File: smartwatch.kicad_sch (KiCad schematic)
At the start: 48 parts, among them IC1 W25N01GVZEIG, IC2 NORA-B120-00B, J1 Charging_Pad-, J2 Charging_Pad+, J3 5022441530, J4 Conn_01x03_Pin, J6 Conn_01x01_Pin, Q1 2N7002, Q2 NTR1P02T1G, Q6 NTR1P02T1G, U1 MAX17048G+T10, U10 AP2127K-1.8, U11 MCP73831-2-OT, U3 MAX30102, U4 DS1302Z+T&R, U5 CAM-M8C-0, U8 AP2112K-3.3TRG1, U9 LIS2DE12, X2 9HT10-32.768KBZC-T, Y1 32.768kHz

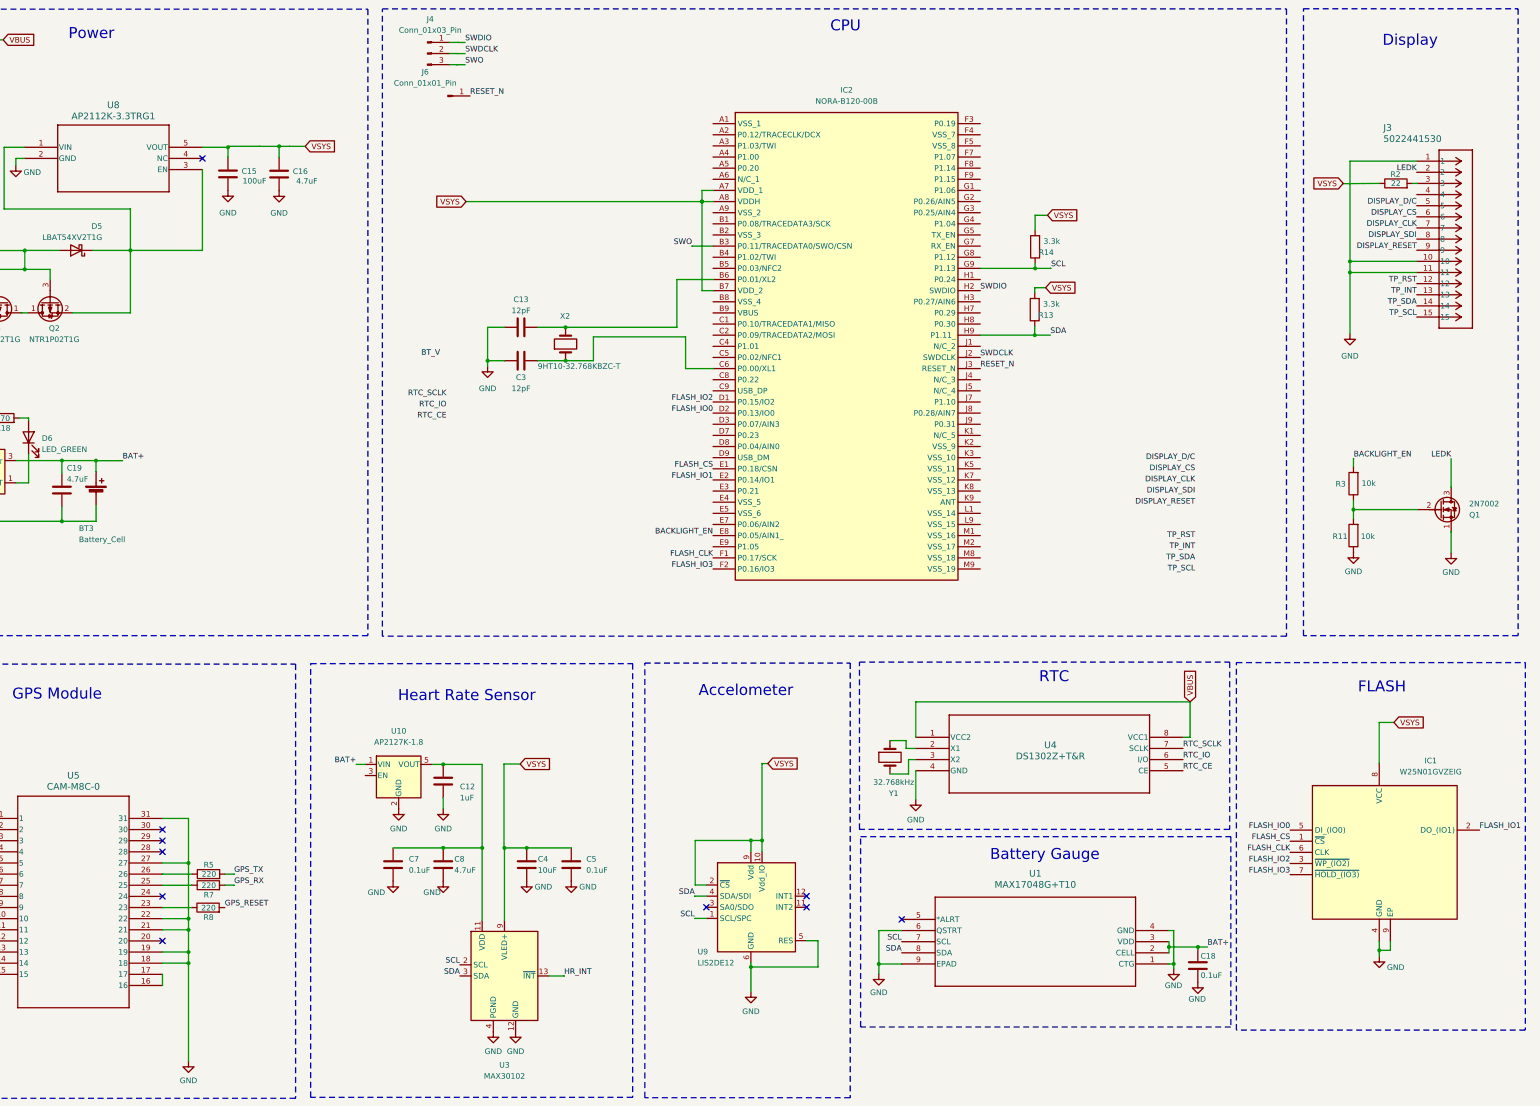
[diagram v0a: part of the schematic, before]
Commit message: switched to 4 layers
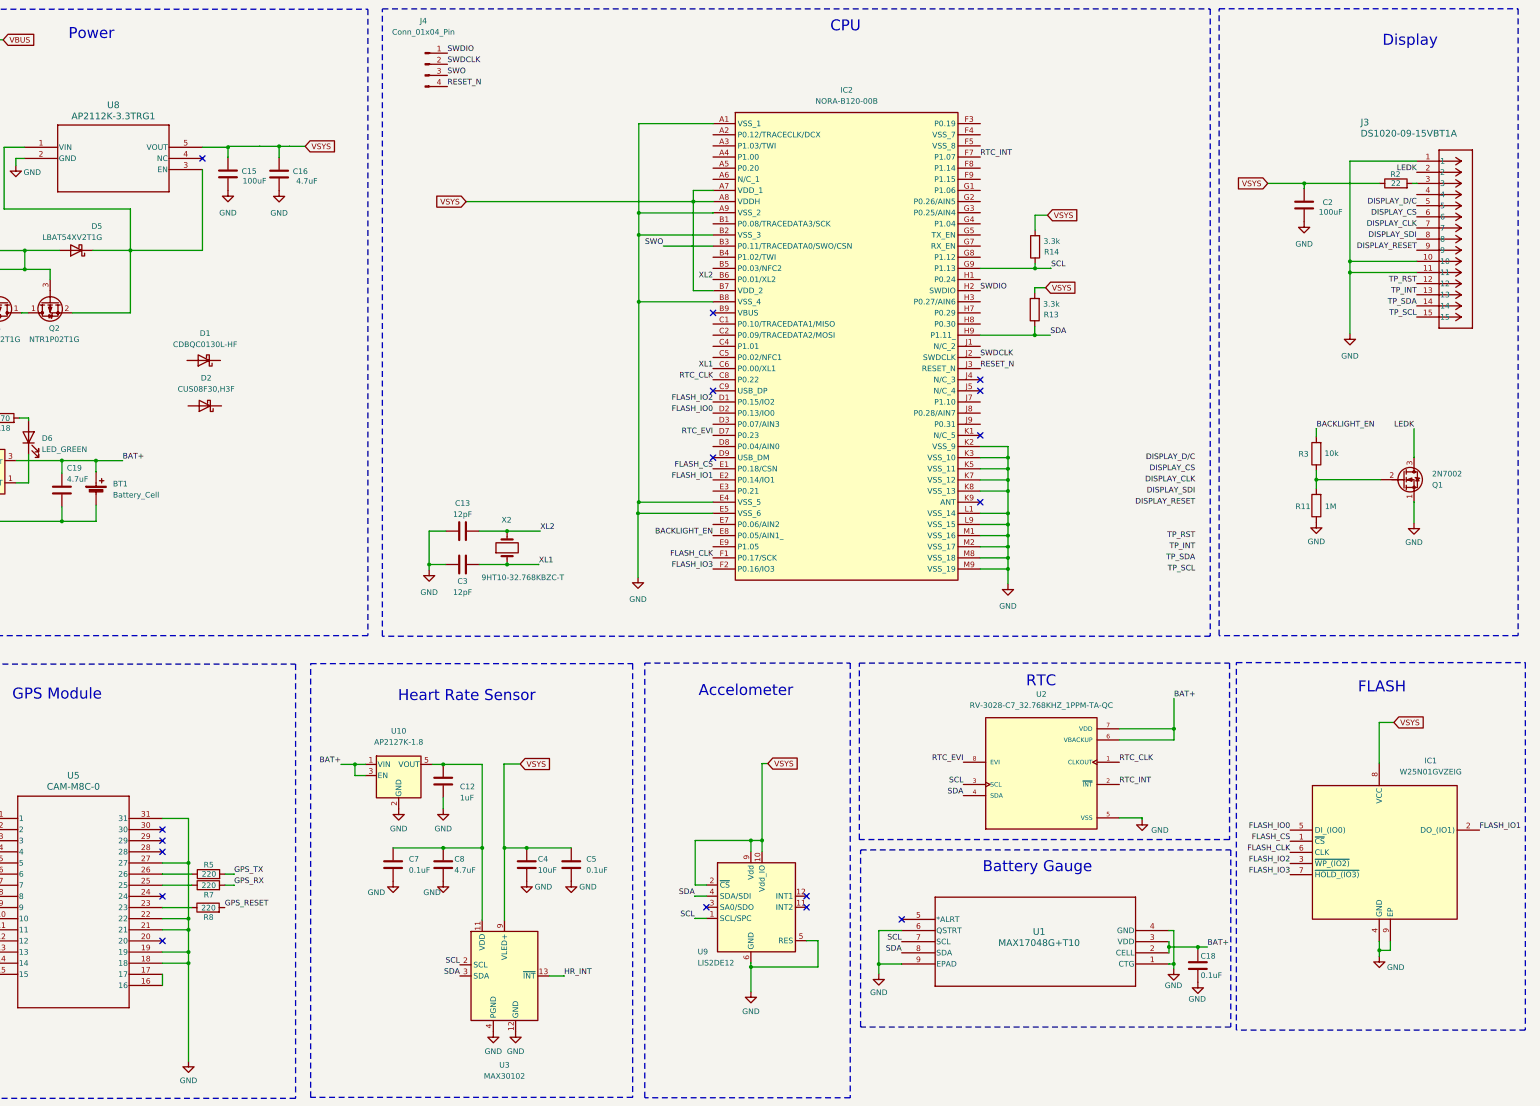
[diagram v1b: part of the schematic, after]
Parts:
- removed J4: Conn_01x03_Pin, Connector_PinSocket_2.54mm:PinSocket_1x03_P2.54mm_Vertical, symbol Connector:Conn_01x03_Pin
- removed J6: Conn_01x01_Pin, Connector_PinSocket_2.54mm:PinSocket_1x01_P2.54mm_Vertical, symbol Connector:Conn_01x01_Pin
- removed U4: DS1302Z+T&R, 21-0041B_8_MXM, symbol DS1302Z+T&R:DS1302Z+T&R
- removed Y1: 32.768kHz, Crystal:Crystal_SMD_TXC_7M-4Pin_3.2x2.5mm, symbol Device:Crystal
- added C2: 100uF, Capacitor_SMD:C_0402_1005Metric, symbol Device:C
- added D1: CDBQC0130L-HF, Diode_SMD:D_SOD-923, symbol Device:D_Schottky
- added D2: CUS08F30,H3F, Diode_SMD:D_SOD-323, symbol Device:D_Schottky
- added J4: Conn_01x04_Pin, Connector_PinHeader_2.54mm:PinHeader_1x04_P2.54mm_Vertical, symbol Connector:Conn_01x04_Pin
- added U2: RV-3028-C7_32.768KHZ_1PPM-TA-QC, RV_3028_C7_32_768KHZ_1PPM_TA_QC:IC_RV-3028-C7_32.768KHZ_1PPM-TA-QC, symbol RV-3028-C7_32.768KHZ_1PPM-TA-QC:RV-3028-C7_32.768KHZ_1PPM-TA-QC
- J3: value 5022441530 -> DS1020-09-15VBT1A; footprint MOLEX_5022441530:CONN_502244-1530_MOL -> DISPLAY_CONNECTOR:FPC-SMD_P0.50-15P_LSXJ-H2.0-15P
- R11: value 10k -> 1M
- renumbered BT3 to BT1
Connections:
- net BAT+: now also U10.3 (EN), U2.6 (VBACKUP), U2.7 (VDD)
- net GND: now also IC2.A1 (VSS_1), IC2.A9 (VSS_2), IC2.B2 (VSS_3), IC2.B8 (VSS_4), IC2.E4 (VSS_5), IC2.E5 (VSS_6), IC2.K2 (VSS_9), IC2.K3 (VSS_10), IC2.K5 (VSS_11), IC2.K7 (VSS_12), IC2.K8 (VSS_13), IC2.L1 (VSS_14), IC2.L9 (VSS_15), IC2.M1 (VSS_16), IC2.M2 (VSS_17), IC2.M8 (VSS_18), IC2.M9 (VSS_19), C2.2, U2.5 (VSS)
- net RESET_N: now also J4.4 (Pin_4)
- net SCL: now also U2.3 (SCL)
- net SDA: now also U2.4 (SDA)
- net SWDCLK: now also J4.2 (Pin_2)
- net SWDIO: now also J4.1 (Pin_1)
- net SWO: now also J4.3 (Pin_3)
- net VSYS: now also C2.1
- net XL1: now reaches C3.2, IC2.C6 (P0.00/XL1), X2.1
- net XL2: now reaches C13.2, IC2.B6 (P0.01/XL2), X2.2
- net RTC_CLK: now reaches IC2.C8 (P0.22)
- net RTC_CLK: now also U2.1 (CLKOUT)
- net RTC_EVI: now reaches IC2.D7 (P0.23)
- net RTC_EVI: now also U2.8 (EVI)
- net RTC_INT: now reaches IC2.F7 (P1.07)
- net RTC_INT: now also U2.2 (~{INT})
- no-connect marks 13 -> 20
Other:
- moved on the sheet: C13, C3, Q1, R11, R3, X2

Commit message: changed backlight resistor values
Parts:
- R2: value 22 -> 100
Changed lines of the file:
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@@
       (effects (font (size 1.27 1.27)))
     )
-    (property "Value" "22" (at 378.014 58.4904 90)
+    (property "Value" "100" (at 378.014 58.4904 90)
       (effects (font (size 1.27 1.27)))
     )

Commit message: worked on power traces & added mounting holes
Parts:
- added C6: 1uF, Capacitor_SMD:C_0402_1005Metric, symbol Device:C
- Q2, Q6: value NTR1P02T1G -> AO3401; footprint Package_TO_SOT_SMD:SOT-23 -> Package_TO_SOT_SMD:SOT-23-3
- R13, R14: value 3.3k -> 4.7k
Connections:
- net GND: now also C6.2
- net at D5.1 (K), Q2.2 (S), U8.1 (VIN)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: now also C6.1
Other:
- moved on the sheet: BT1, C1, C15, C16, C19, D1, D2, D5, D6, J1, J2, Q2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

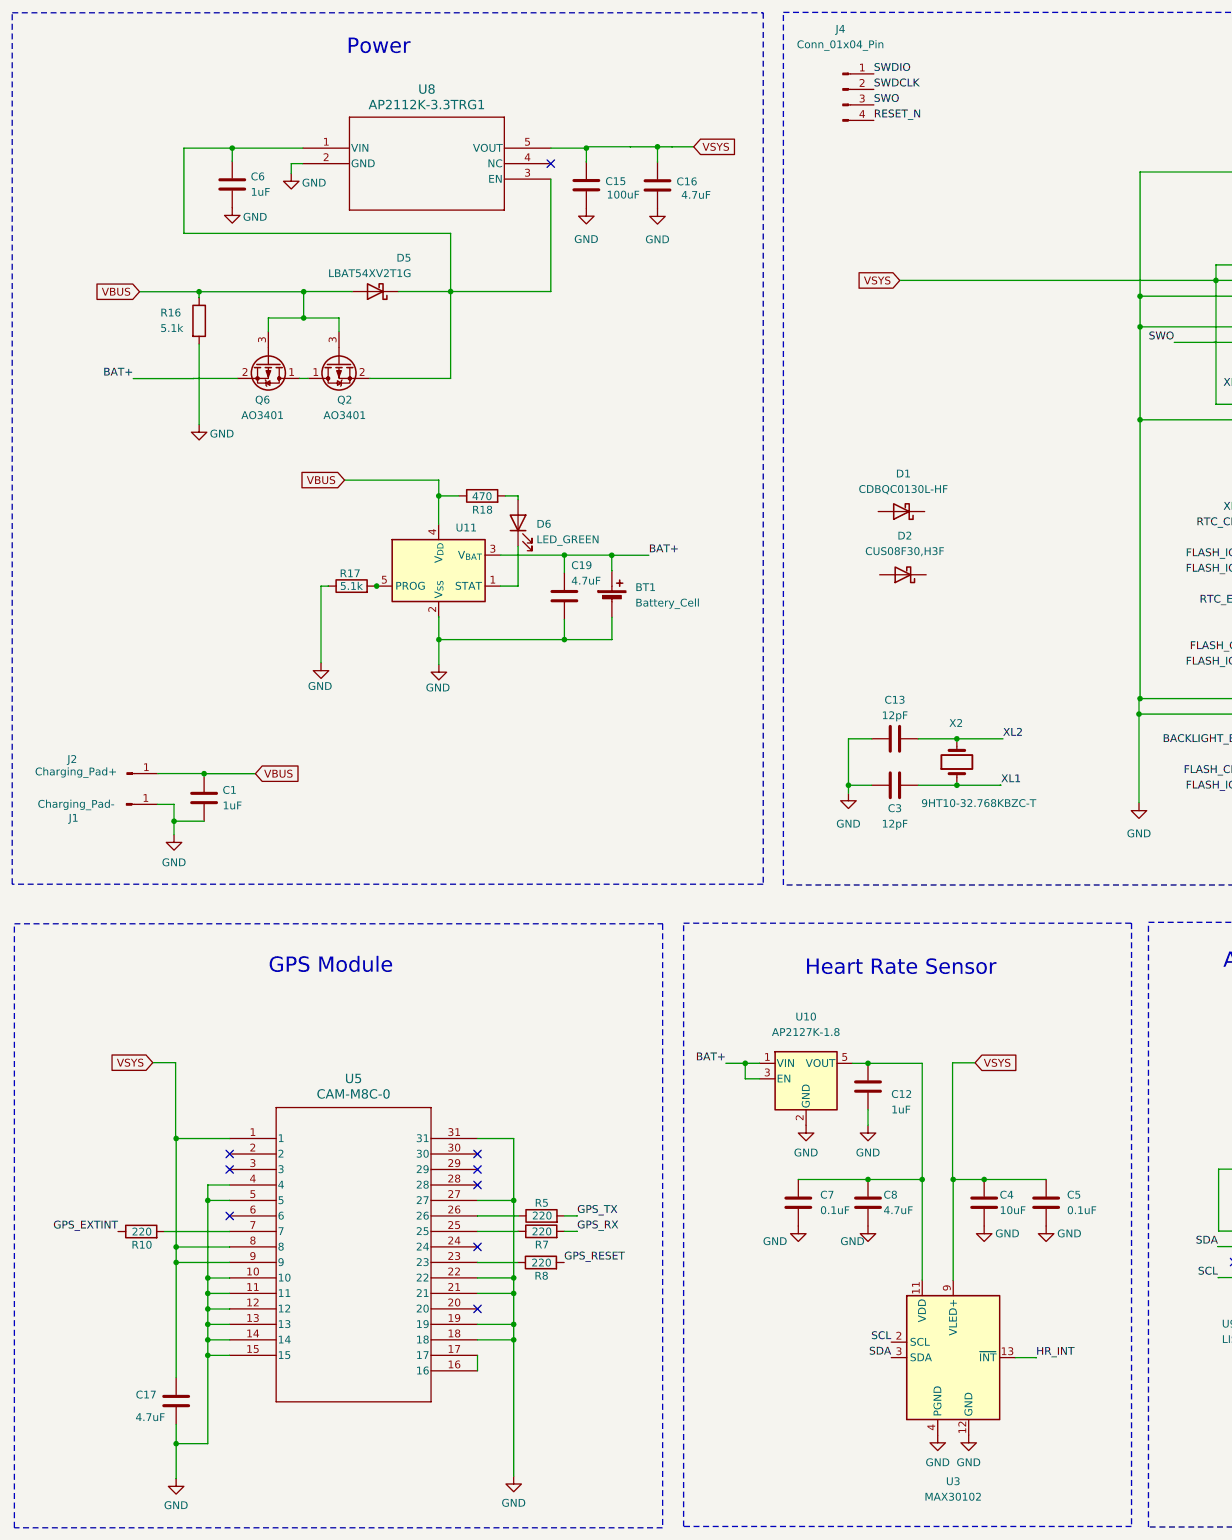
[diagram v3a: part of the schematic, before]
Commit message: added lm66200
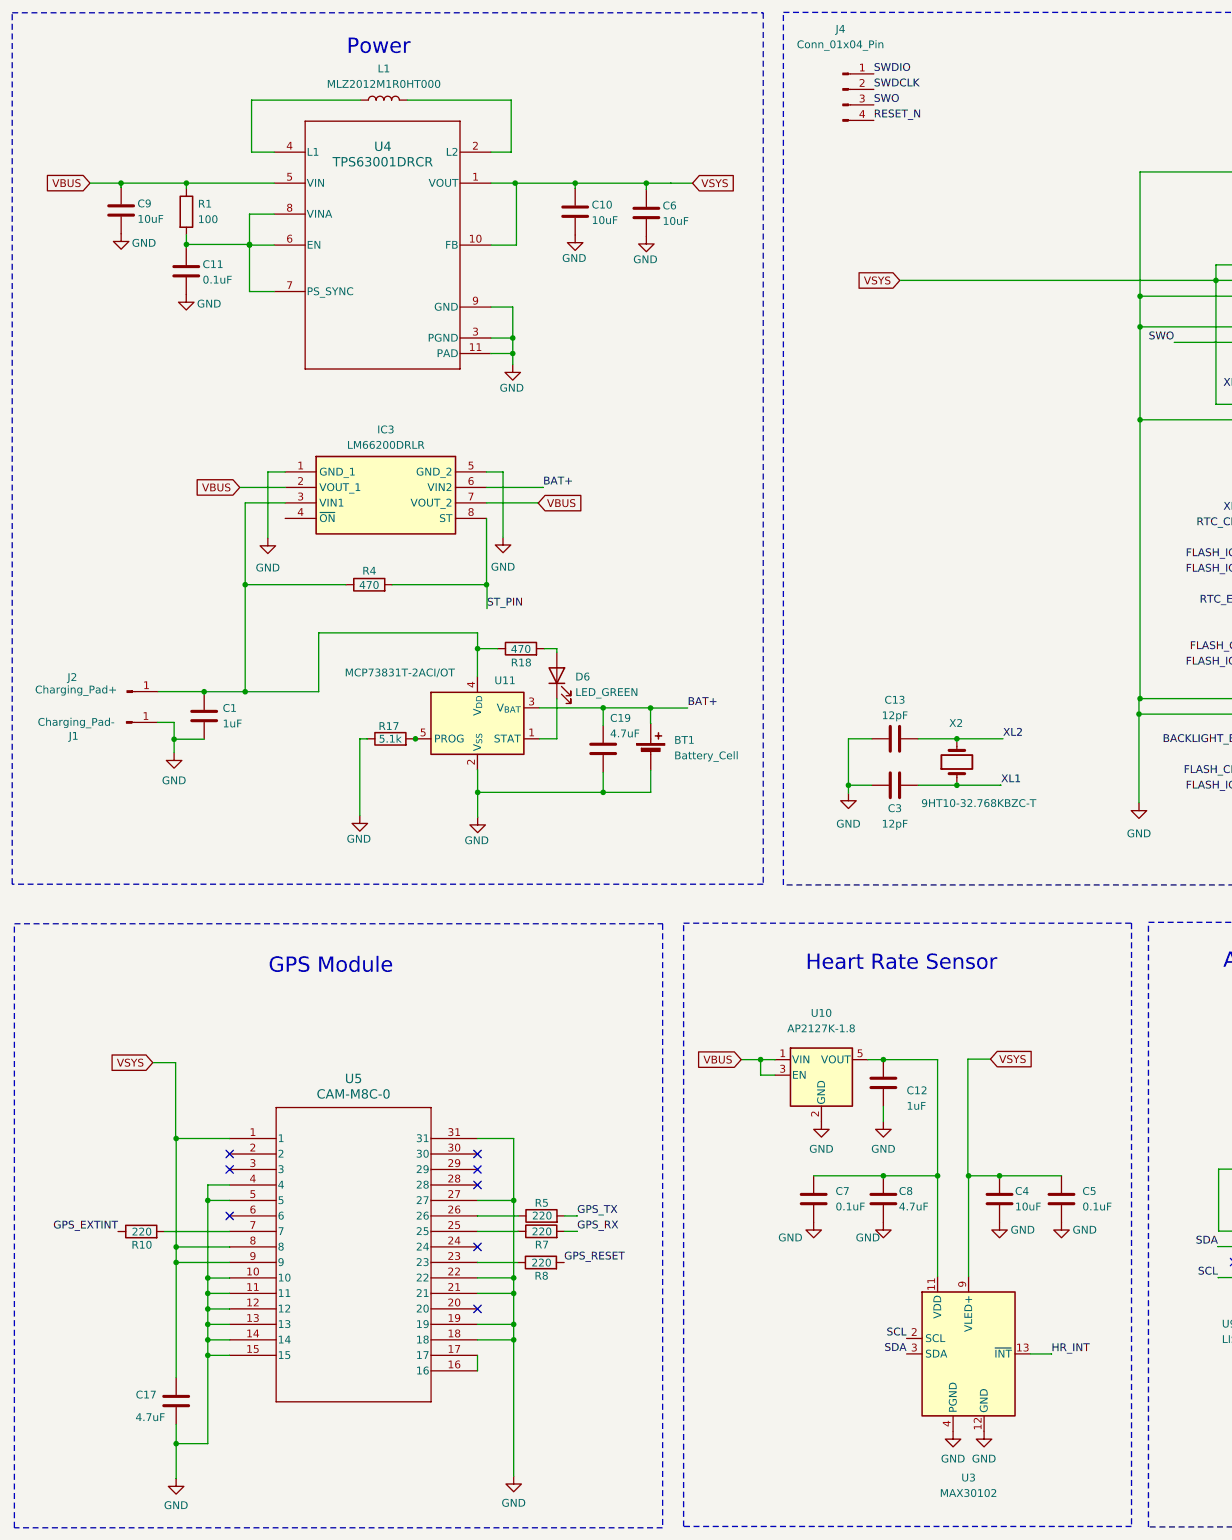
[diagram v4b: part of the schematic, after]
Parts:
- removed C15: 100uF, Capacitor_SMD:C_0402_1005Metric, symbol Device:C
- removed C16: 4.7uF, Capacitor_Tantalum_SMD:CP_EIA-2012-12_Kemet-R, symbol Device:C
- removed D1: CDBQC0130L-HF, Diode_SMD:D_SOD-923, symbol Device:D_Schottky
- removed D2: CUS08F30,H3F, Diode_SMD:D_SOD-323, symbol Device:D_Schottky
- removed D5: LBAT54XV2T1G, Diode_SMD:D_SOD-523, symbol Device:D_Schottky
- removed Q2, Q6: AO3401, Package_TO_SOT_SMD:SOT-23-3, symbol Device:Q_PMOS_DSG
- removed R16: 5.1k, Resistor_SMD:R_0603_1608Metric, symbol Device:R
- removed U8: AP2112K-3.3TRG1, AP2112K-3-3TRG1:SOT_RG1_DIO, symbol AP2112K-3-3TRG1:AP2112K-3.3TRG1
- added C10, C9: 10uF, Capacitor_SMD:C_0402_1005Metric, symbol Device:C
- added C11: 0.1uF, Capacitor_SMD:C_0402_1005Metric, symbol Device:C
- added IC3: LM66200DRLR, LM66200DRLR:SOTFL50P160X60-8N, symbol LM66200DRLR:LM66200DRLR
- added L1: MLZ2012M1R0HT000, Inductor_SMD:L_0805_2012Metric, symbol Device:L
- added R1: 100, Resistor_SMD:R_0402_1005Metric, symbol Device:R
- added R4: 470, Resistor_SMD:R_0402_1005Metric, symbol Device:R
- added U4: TPS63001DRCR, DRC0010J, symbol TPS63001DRCR:TPS63001DRCR
- C6: value 1uF -> 10uF
- U11: value MCP73831-2-OT -> MCP73831T-2ACI/OT
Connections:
- net BAT+: now also IC3.6 (VIN2); no longer U10.1 (VIN), U10.3 (EN)
- net GND: now also C10.2, C11.2, C9.2, IC3.1 (GND_1), IC3.5 (GND_2), U4.11 (PAD), U4.3 (PGND), U4.9 (GND)
- net VBUS: now also U10.1 (VIN), U10.3 (EN), C9.1, IC3.2 (VOUT_1), IC3.7 (VOUT_2), R1.1, U4.5 (VIN); no longer C1.1, J2.1 (Pin_1), R18.1, U11.4 (V_{DD})
- net VSYS: now also C6.1, C10.1, U4.1 (VOUT), U4.10 (FB)
- new net: C11.1, R1.2, U4.6 (EN), U4.7 (PS_SYNC), U4.8 (VINA)
- new net: C1.1, IC3.3 (VIN1), J2.1 (Pin_1), R18.1, R4.1, U11.4 (V_{DD})
- new net: L1.1, U4.4 (L1)
- new net: L1.2, U4.2 (L2)
- new net ST_PIN: IC3.8 (ST), R4.2
- no-connect marks 20 -> 19
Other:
- moved on the sheet: BT1, C1, C12, C19, C4, C5, C7, C8, D6, J1, J2, R17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

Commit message: signal routing 50% complete
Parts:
- removed C12: 1uF, Capacitor_SMD:C_0402_1005Metric, symbol Device:C
- removed C2: 100uF, Capacitor_SMD:C_0402_1005Metric, symbol Device:C
- removed U10: AP2127K-1.8, Package_TO_SOT_SMD:SOT-23-5, symbol Regulator_Linear:AP2127K-1.8
- added R12, R15, R6, R9: 4.7k, Resistor_SMD:R_0402_1005Metric, symbol Device:R
- added U6: AP7313-18SAG-7, SOT-23_DIO, symbol AP7313-18SAG-7:AP7313-18SAG-7
- R4: value 470 -> 4.7k; MPN (none) -> NRF52840-QIAA-R
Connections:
- net BACKLIGHT_EN: now also IC2.D3 (P0.07/AIN3); no longer IC2.E8 (P0.05/AIN1_)
- net DISPLAY_CLK: now also IC2.G8 (P1.12)
- net DISPLAY_CS: now also IC2.H7 (P0.29)
- net DISPLAY_D/C: now also IC2.H8 (P0.30)
- net DISPLAY_RESET: now also IC2.F7 (P1.07)
- net DISPLAY_SDI: now also IC2.F8 (P1.14)
- net GND: now also IC3.4 (~{ON}), J3.4, U6.3 (GND)
- net GPS_EXTINT: now also IC2.B5 (P0.03/NFC2)
- net GPS_RESET: now also IC2.A2 (P0.12/TRACECLK/DCX)
- net GPS_RX: now also IC2.A5 (P0.20)
- net GPS_TX: now also IC2.A4 (P1.00)
- net HR_INT: now also R9.1
- net RTC_CLK: now also IC2.J8 (P0.28/AIN7); no longer IC2.C8 (P0.22)
- net RTC_EVI: now also IC2.J9 (P0.31); no longer IC2.D7 (P0.23)
- net RTC_INT: now also IC2.J7 (P1.10); no longer IC2.F7 (P1.07)
- net TP_INT: now also IC2.D8 (P0.04/AIN0), R6.1
- net TP_RST: now also IC2.E8 (P0.05/AIN1_), R12.1
- net TP_SCL: now also IC2.B4 (P1.02/TWI), IC2.D7 (P0.23), R4.1
- net TP_SDA: now also IC2.A3 (P1.03/TWI), IC2.E7 (P0.06/AIN2), R15.1
- net VBUS: now also U6.1 (IN)
- net at C1.1, IC3.3 (VIN1), J2.1 (Pin_1)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: no longer R4.1
- net +1V8: now reaches C7.1, C8.1, U3.11 (VDD)
- net +1V8: now also U6.2 (OUT)
- net ST_PIN: no longer names the net of IC3.8 (ST)
- net ST_PIN: no longer R4.2
- net VSYS renamed +3.3V
- net +3.3V: now also R4.2, R12.2, R15.2, R6.2, R9.2
- no-connect marks 19 -> 21
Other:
- note added: "Charging Circuit"
- note added: "Heart-Rate Sensor"
- note added: "MCU"
- note added: "NRF5340 Smartwatch"
- note added: "Regulators"
- note removed: "CPU"
- note removed: "Heart Rate Sensor"
- note removed: "Power"
- moved on the sheet: BT1, C1, C10, C11, C17, C19, C4, C5, C6, C7, C8, C9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

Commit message: ready for production
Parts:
- removed C13, C3: 12pF, Capacitor_SMD:C_0402_1005Metric, symbol Device:C
- added R16, R19, R20, R21: 4.7k, Resistor_SMD:R_0402_1005Metric, symbol Device:R
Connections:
- net +3.3V: now also J3.4, R16.2, R20.2, R21.2
- net BAT+: now also R19.2
- net FLASH_CS: now also R16.1
- net FLASH_IO2: now also R20.1
- net FLASH_IO3: now also R21.1
- net GND: no longer J3.4
- net RTC_INT: now also R19.1
- net TP_SCL: no longer IC2.B4 (P1.02/TWI)
- net TP_SDA: no longer IC2.A3 (P1.03/TWI)
- net XL1: now also X2.2; no longer X2.1
- net XL2: now also X2.1; no longer X2.2
- no-connect marks 21 -> 44
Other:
- moved on the sheet: C18, J4, U1, U2, X2
